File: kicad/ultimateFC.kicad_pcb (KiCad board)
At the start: 8 copper layers, 30.4 x 25.2 mm, 192 parts, among them J1 USB_B_Micro, J2 10132797-011100LF, J3 10132797-011100LF, J4 10132797-011100LF, J5 10132797-011100LF, J6 10132797-011100LF, Q1 DMP2066LSN-7, U1 EFM8BB21F16G-C-QFN20R, U10 NCP81253MNTBG, U11 SiZ200DT, U12 NCP81253MNTBG, U13 SiZ200DT, U14 TPS62821, U15 SiZ200DT, U16 NCP81253MNTBG, U17 NCP81253MNTBG, U18 NCP81253MNTBG, U19 NCP81253MNTBG, U2 EFM8BB21F16G-C-QFN20R, U20 SiZ200DT, U21 SiZ200DT, U22 SiZ200DT, U23 SiZ200DT, U24 EFM8BB21F16G-C-QFN20R, U25 NCP81253MNTBG, U26 SiZ200DT, U27 NCP81253MNTBG, U28 NCP81253MNTBG, U29 SiZ200DT, U3 NCP81253MNTBG, U30 SiZ200DT, U31 INA186, U32 LMR33630CQRNX, U33 STM32F745VGHx, U34 AB7456, U35 ZOE-M8Q_ZOE-M8Q, U36 ICM-20602, U37 S25FL064L, U39 BMP280, U4 SiZ200DT, U6 EFM8BB21F16G-C-QFN20R, U7 NCP81253MNTBG, U8 SiZ200DT, U9 NCP81253MNTBG, X1 Molex_734120110, Y1 CSTNE8M00G550000R0, Y2 ECS-270-8-47Q-CES-TR

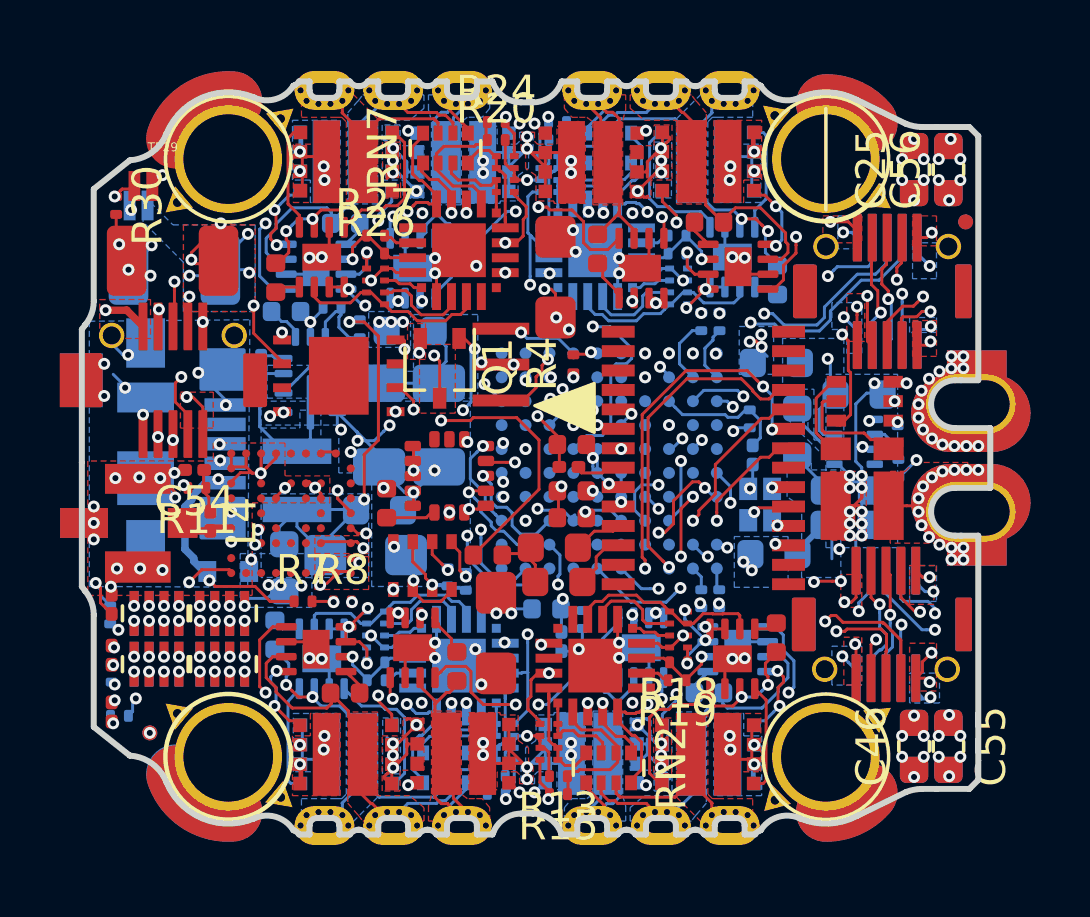
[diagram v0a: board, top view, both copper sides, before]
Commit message: changed motor pins for more TIMER/ DMA / ADC Support
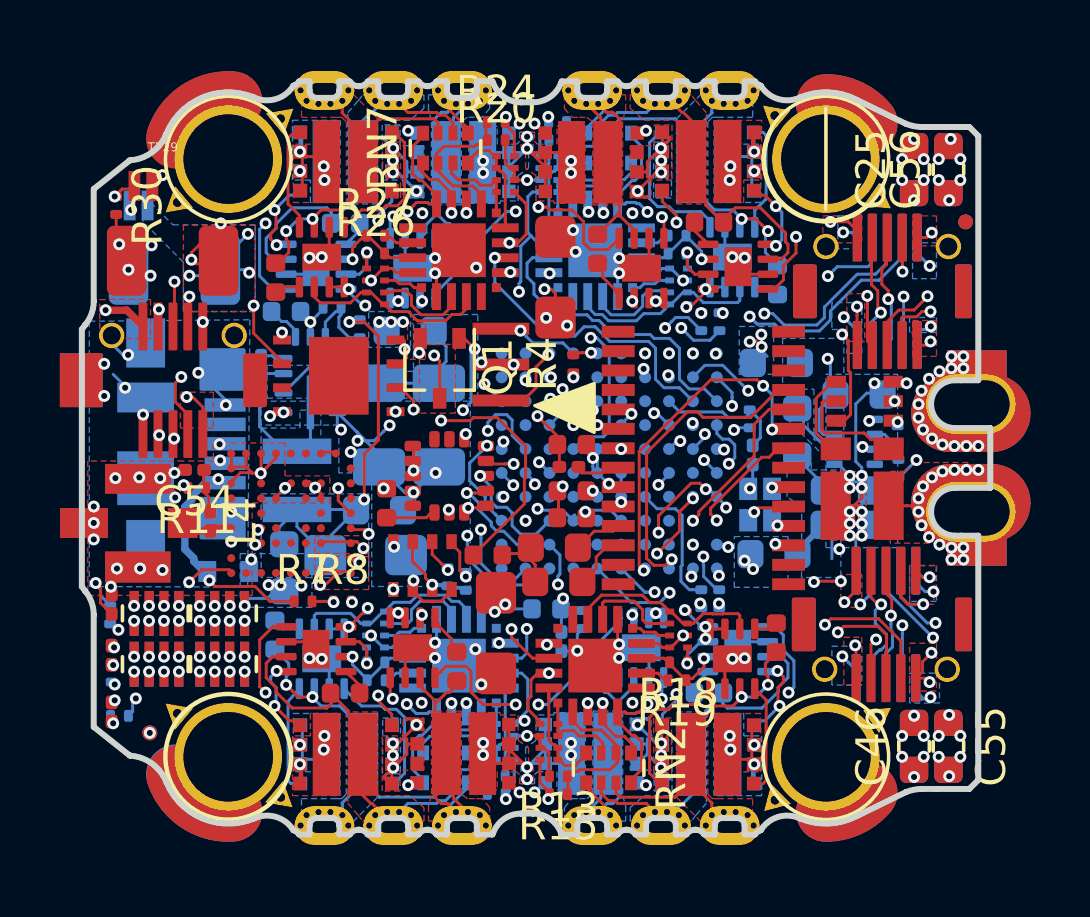
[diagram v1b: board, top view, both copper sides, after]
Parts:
- removed the REF** at (197.1, 64.1) (x2)
- added REF**: Fiducial_0.5mm_Dia_1mm_Outer, Fiducial:Fiducial_0.5mm_Dia_1mm_Outer, F.Cu at (197.1, 64.1)
- added REF**: Fiducial_0.5mm_Dia_1mm_Outer, Fiducial:Fiducial_0.5mm_Dia_1mm_Outer, B.Cu at (197.1, 64.1)
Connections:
- net CS_BERGSTAK20 renamed Net-(U33-PadG3)
- U33 pad A5: UART1_RX -> MP_PIN6
- U33 pad B5: UART1_TX -> MP_PIN5
- U33 pad B6: /USART2_TX -> UART2_TX
- U33 pad C6: Net-(U33-PadC6) -> UART2_RX
- U33 pad G7: MP_PIN4 -> ESC4_RX
- U33 pad G8: MP_PIN6 -> /TIM4_CH4
- U33 pad H6: Net-(U33-PadH6) -> ESC3_RX
- U33 pad H8: MP_PIN5 -> /TIM4_CH3
- U33 pad J10: ESC4_RX -> ESC_4_TX
- U33 pad J2: ESC2_RX -> MP_PIN3
- U33 pad J3: MP_PIN3 -> ESC_2_TX
- U33 pad J4: Net-(U33-PadJ4) -> MP_PIN1
- U33 pad K10: ESC3_RX -> ESC_3_TX
- U33 pad K2: ESC1_RX -> MP_PIN2
- U33 pad K3: MP_PIN1 -> ESC_1_TX
- U33 pad K4: Net-(U33-PadK4) -> MP_PIN4
- U33 pad K5: Net-(U33-PadK5) -> ESC1_RX
- U33 pad K6: MP_PIN2 -> ESC2_RX
- U35 pad P$J4: UART1_TX -> UART2_TX
- U35 pad P$J5: UART1_RX -> UART2_RX
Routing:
- net ESC_3_TX: track 0.00 -> 10.5 mm, vias 0 -> 2
- net ESC_1_TX: track 0.00 -> 10.1 mm
- net ESC_2_TX: track 0.00 -> 9.97 mm, vias 0 -> 1
- net UART2_RX: track 0.00 -> 9.63 mm, vias 0 -> 2
- net UART2_TX: track 0.00 -> 8.15 mm, vias 0 -> 2
- net ESC_4_TX: track 0.00 -> 8.13 mm, vias 0 -> 2
- net MP_PIN6: track 20.7 -> 12.8 mm
- net UART1_RX: track 7.87 -> 0.00 mm, vias 2 -> 0
- net ESC1_RX: track 1.93 -> 9.74 mm, vias 0 -> 2
- net MP_PIN5: track 22.2 -> 14.7 mm
- net ESC2_RX: track 2.22 -> 9.59 mm, vias 0 -> 2
- net UART1_TX: track 7.11 -> 0.00 mm, vias 2 -> 0
- net MP_PIN2: track 11.4 -> 17.5 mm
- net ESC3_RX: track 0.70 -> 5.22 mm, vias 0 -> 2
- net MP_PIN4: track 13.4 -> 17.2 mm
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
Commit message: Cleaned up a bit
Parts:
- removed the REF** at (197.1, 64.1) (x2)
- added REF**: Fiducial_0.5mm_Dia_1mm_Outer, Fiducial:Fiducial_0.5mm_Dia_1mm_Outer, F.Cu at (197.1, 64.1)
- added REF**: Fiducial_0.5mm_Dia_1mm_Outer, Fiducial:Fiducial_0.5mm_Dia_1mm_Outer, B.Cu at (197.1, 64.1)

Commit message: added images
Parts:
- removed the REF** at (197.1, 64.1) (x2)
- added REF**: Fiducial_0.5mm_Dia_1mm_Outer, Fiducial:Fiducial_0.5mm_Dia_1mm_Outer, F.Cu at (197.1, 64.1)
- added REF**: Fiducial_0.5mm_Dia_1mm_Outer, Fiducial:Fiducial_0.5mm_Dia_1mm_Outer, B.Cu at (197.1, 64.1)
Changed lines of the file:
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@@
     (polygon
       (pts
-        (xy 174.9 70.4) (xy 175.6 70.4) (xy 175.6 71.8) (xy 173.6 71.8) (xy 173.6 71)
-        (xy 174.9 71)
+        (xy 174.9 70.4) (xy 175.6 70.4) (xy 175.6 71.8) (xy 173.6 71.8) (xy 173.6 71.3)
+        (xy 174.9 71.3)
       )
     )

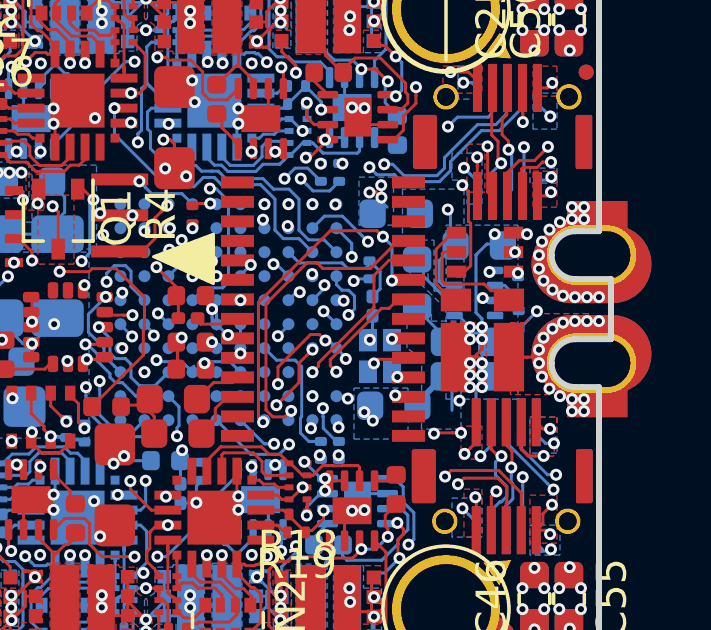
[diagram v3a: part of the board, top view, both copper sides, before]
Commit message: changed 3.3V dcdc converter to one with forced pwm
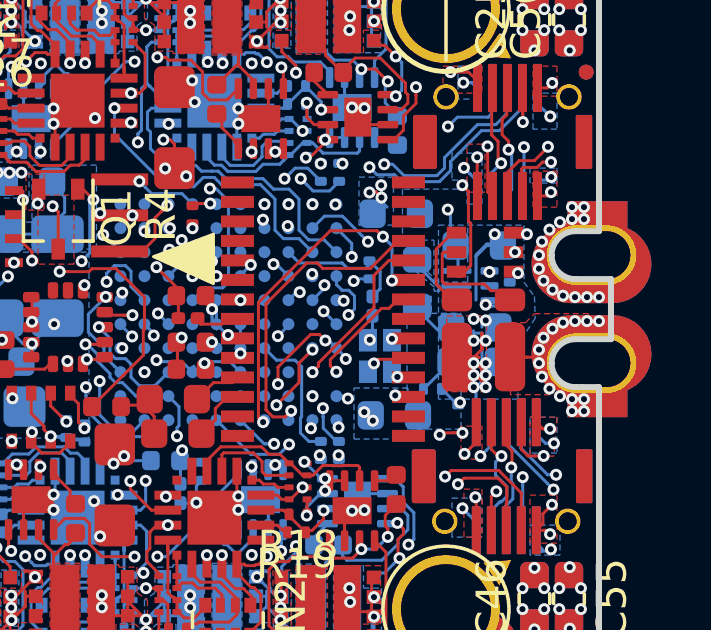
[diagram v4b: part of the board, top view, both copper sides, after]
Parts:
- removed the REF** at (197.1, 64.1) (x2)
- added C53: 120pF, ultimateFC:R_0201_0603Metric_mod, B.Cu at (192.1, 74.7)
- added REF**: Fiducial_0.5mm_Dia_1mm_Outer, Fiducial:Fiducial_0.5mm_Dia_1mm_Outer, F.Cu at (197.1, 64.1)
- added REF**: Fiducial_0.5mm_Dia_1mm_Outer, Fiducial:Fiducial_0.5mm_Dia_1mm_Outer, B.Cu at (197.1, 64.1)
- U14: value TPS62821 -> TPS62824ADMQ; footprint ultimateFC:VSON-8HR -> ultimateFC:VSON_HR6
- moved R21 3.24 mm to (192.9, 74.9), turned to 270 degrees
- moved C11 0.54 mm to (193.5, 72.6)
- moved C8 0.53 mm to (193.4, 73.8)
- moved R22 0.33 mm to (194.6, 71.4)
- moved FB4 0.32 mm to (190.8, 75.5)
- moved U14 0.28 mm to (193.3, 71.2)
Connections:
- R21 pad 2: Net-(R21-Pad2) -> Net-(C53-Pad2)
- R22 pad 1: Net-(R21-Pad2) -> Net-(C53-Pad2)
- U14 pad 2: Net-(R21-Pad2) -> Net-(U14-Pad2)
- U14 pad 3: GND -> Net-(C53-Pad2)
- U14 pad 4: Net-(U14-Pad4) -> GND
- U14 pad 5: GND -> Net-(L2-Pad1)
- U14 pad 6: Net-(L2-Pad1) -> Net-(C6-Pad1)
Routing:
- net Net-(C53-Pad2): track 0.00 -> 5.83 mm, vias 0 -> 2
- net Net-(C11-Pad1): track 10.6 -> 5.48 mm, vias 2 -> 0
- net Net-(R21-Pad2): track 1.43 -> 0.00 mm
- net Net-(C6-Pad1): track 6.20 -> 4.93 mm
- net I2C_SDA: track 40.5 -> 39.7 mm
- net Net-(L2-Pad1): track 1.64 -> 0.84 mm
- net GND: track 143.7 -> 143.1 mm, vias 152 -> 151
